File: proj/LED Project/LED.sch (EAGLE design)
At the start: 0 parts

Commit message: Started Schematic
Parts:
- added Q1: (no value), crystal:CRYSTALCTS406
- added R1: 1M, rcl:R-US_R0603
- added U1: ATMEGA328P-AUR, ATMEGA328P-AUR:ATMEGA328P-AUR
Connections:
- new net N$1: Q1.1, R1.2, U1.PB6(PCINT6/XTAL1/TOSC1)
- new net N$2: Q1.2, R1.1, U1.PB7(PCINT7/XTAL2/TOSC2)
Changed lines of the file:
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@@
 <grid distance="0.1" unitdist="inch" unit="inch" style="lines" multiple="1" display="no" altdistance="0.01" altunitdist="inch" altunit="inch"/>
 <layers>
+<layer number="1" name="Top" color="4" fill="1" visible="no" active="no"/>
+<layer number="16" name="Bottom" color="1" fill="1" visible="no" active="no"/>
+<layer number="17" name="Pads" color="2" fill="1" visible="no" active="no"/>
+<layer number="18" name="Vias" color="2" fill="1" visible="no" active="no"/>
+<layer number="19" name="Unrouted" color="6" fill="1" visible="no" active="no"/>
+<layer number="20" name="Dimension" color="15" fill="1" visible="no" active="no"/>
+<layer number="21" name="tPlace" color="7" fill="1" visible="no" active="no"/>
+<layer number="22" name="bPlace" color="7" fill="1" visible="no" active="no"/>
+<layer number="23" name="tOrigins" color="15" fill="1" visible="no" active="no"/>
+<layer number="24" name="bOrigins" color="15" fill="1" visible="no" active="no"/>
+<layer number="25" name="tNames" color="7" fill="1" visible="no" active="no"/>
+<layer number="26" name="bNames" color="7" fill="1" visible="no" active="no"/>
+<layer number="27" name="tValues" color="7" fill="1" visible="no" active="no"/>
+<layer number="28" name="bValues" color="7" fill="1" visible="no" active="no"/>
+<layer number="29" name="tStop" color="7" fill="3" visible="no" active="no"/>
+<layer number="30" name="bStop" color="7" fill="6" visible="no" active="no"/>
+<layer number="31" name="tCream" color="7" fill="4" visible="no" active="no"/>
+<layer number="32" name="bCream" color="7" fill="5" visible="no" active="no"/>
+<layer number="33" name="tFinish" color="6" fill="3" visible="no" active="no"/>
+<layer number="34" name="bFinish" color="6" fill="6" visible="no" active="no"/>
+<layer number="35" name="tGlue" color="7" fill="4" visible="no" active="no"/>
+<layer number="36" name="bGlue" color="7" fill="5" visible="no" active="no"/>
+<layer number="37" name="tTest" color="7" fill="1" visible="no" active="no"/>
+<layer number="38" name="bTest" color="7" fill="1" visible="no" active="no"/>
+<layer number="39" name="tKeepout" color="4" fill="11" visible="no" active="no"/>
+<layer number="40" name="bKeepout" color="1" fill="11" visible="no" active="no"/>
+<layer number="41" name="tRestrict" color="4" fill="10" visible="no" active="no"/>
+<layer number="42" name="bRestrict" color="1" fill="10" visible="no" active="no"/>
+<layer number="43" name="vRestrict" color="2" fill="10" visible="no" active="no"/>
+<layer number="44" name="Drills" color="7" fill="1" visible="no" active="no"/>
+<layer number="45" name="Holes" color="7" fill="1" visible="no" active="no"/>
+<layer number="46" name="Milling" color="3" fill="1" visible="no" active="no"/>
+<layer number="47" name="Measures" color="7" fill="1" visible="no" active="no"/>
+<layer number="48" name="Document" color="7" fill="1" visible="no" active="no"/>
+<layer number="49" name="Reference" color="7" fill="1" visible="no" active="no"/>
+<layer number="51" name="tDocu" color="7" fill="1" visible="no" active="no"/>
+<layer number="52" name="bDocu" color="7" fill="1" visible="no" active="no"/>
 <layer number="88" name="SimResults" color="9" fill="1" visible="yes" active="yes"/>
 <layer number="89" name="SimProbes" color="9" fill="1" visible="yes" active="yes"/>
@@
 </classes>
 <parts>
+<part name="U1" library="ATMEGA328P-AUR" deviceset="ATMEGA328P-AUR" device=""/>
+<part name="R1" library="rcl" library_urn="urn:adsk.eagle:library:334" deviceset="R-US_" device="R0603" package3d_urn="urn:adsk.eagle:package:23555/2" value="1M"/>
+<part name="Q1" library="crystal" library_urn="urn:adsk.eagle:library:204" deviceset="CRYSTAL" device="CTS406" package3d_urn="urn:adsk.eagle:package:12089/1"/>
 </parts>
 <sheets>
@@
 </plain>
 <instances>
+<instance part="U1" gate="G$1" x="73.66" y="40.64"/>
+<instance part="R1" gate="G$1" x="30.48" y="38.1" rot="R90"/>
+<instance part="Q1" gate="G$1" x="20.32" y="38.1" rot="R270"/>
 </instances>
 <busses>
 </busses>
 <nets>
+<net name="N$1" class="0">
+<segment>
+<pinref part="U1" gate="G$1" pin="PB6(PCINT6/XTAL1/TOSC1)"/>
+<wire x1="38.1" y1="40.64" x2="33.02" y2="40.64" width="0.1524" layer="91"/>
+<wire x1="33.02" y1="40.64" x2="33.02" y2="43.18" width="0.1524" layer="91"/>
+<pinref part="R1" gate="G$1" pin="2"/>
+<wire x1="33.02" y1="43.18" x2="30.48" y2="43.18" width="0.1524" layer="91"/>
+<pinref part="Q1" gate="G$1" pin="1"/>
+<wire x1="30.48" y1="43.18" x2="20.32" y2="43.18" width="0.1524" layer="91"/>
+<junction x="30.48" y="43.18"/>
+<wire x1="20.32" y1="40.64" x2="20.32" y2="43.18" width="0.1524" layer="91"/>
+</segment>
+</net>
+<net name="N$2" class="0">
+<segment>
+<pinref part="U1" gate="G$1" pin="PB7(PCINT7/XTAL2/TOSC2)"/>
+<wire x1="38.1" y1="38.1" x2="33.02" y2="38.1" width="0.1524" layer="91"/>
+<wire x1="33.02" y1="38.1" x2="33.02" y2="33.02" width="0.1524" layer="91"/>
+<pinref part="R1" gate="G$1" pin="1"/>
+<wire x1="33.02" y1="33.02" x2="30.48" y2="33.02" width="0.1524" layer="91"/>
+<pinref part="Q1" gate="G$1" pin="2"/>
+<wire x1="20.32" y1="35.56" x2="20.32" y2="33.02" width="0.1524" layer="91"/>
+<wire x1="20.32" y1="33.02" x2="30.48" y2="33.02" width="0.1524" layer="91"/>
+<junction x="30.48" y="33.02"/>
+</segment>
+</net>
 </nets>
 </sheet>
@@
 </schematic>
 </drawing>
+<compatibility>
+<note version="8.2" severity="warning">
+Since Version 8.2, EAGLE supports online libraries. The ids
+of those online libraries will not be understood (or retained)
+with this version.
+</note>
+<note version="8.3" severity="warning">
+Since Version 8.3, EAGLE supports URNs for individual library
+assets (packages, symbols, and devices). The URNs of those assets
+will not be understood (or retained) with this version.
+</note>
+<note version="8.3" severity="warning">
+Since Version 8.3, EAGLE supports the association of 3D packages
+with devices in libraries, schematics, and board files. Those 3D
+packages will not be understood (or retained) with this version.
+</note>
+<note version="8.4" severity="warning">
+Since Version 8.4, EAGLE supports properties for SPICE simulation.
+Probes in schematics and SPICE mapping objects found in parts and library devices
+will not be understood with this version. Update EAGLE to the latest version
+for full support of SPICE simulation.
+</note>
+</compatibility>
 </eagle>

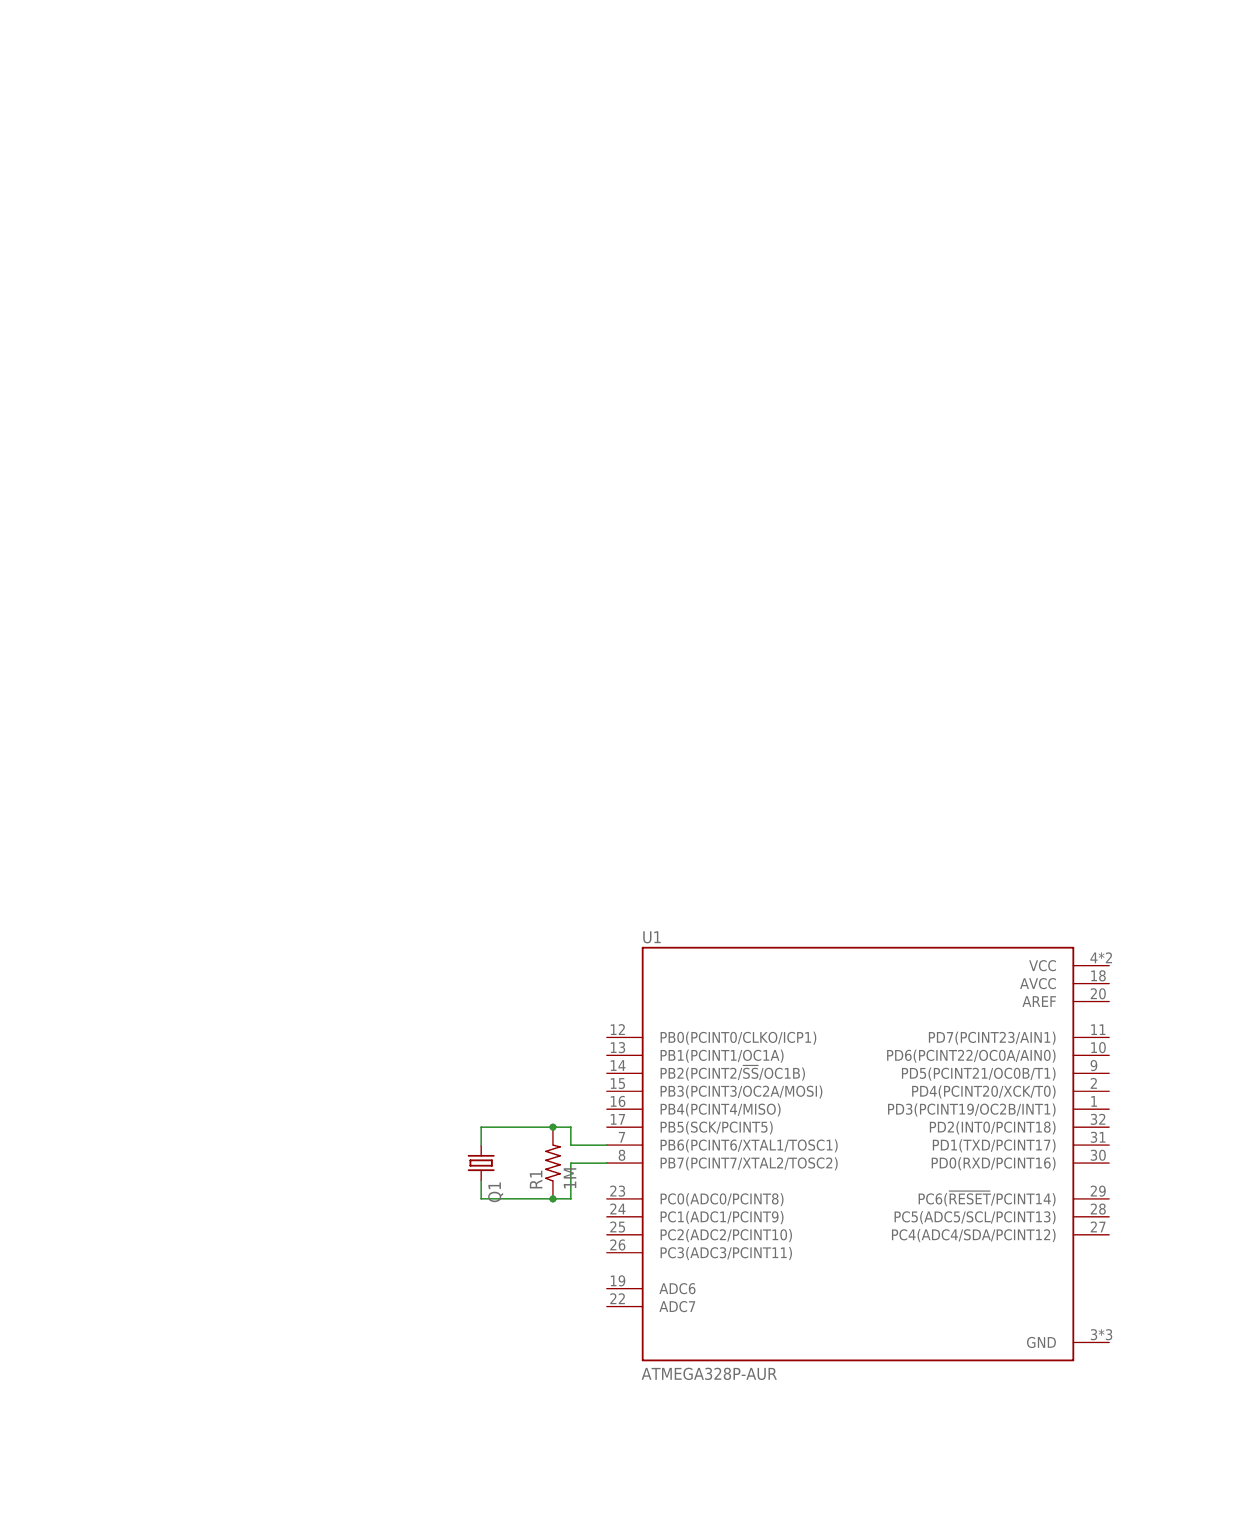
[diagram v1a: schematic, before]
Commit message: Working on the Schematic for a BareBones Arduino
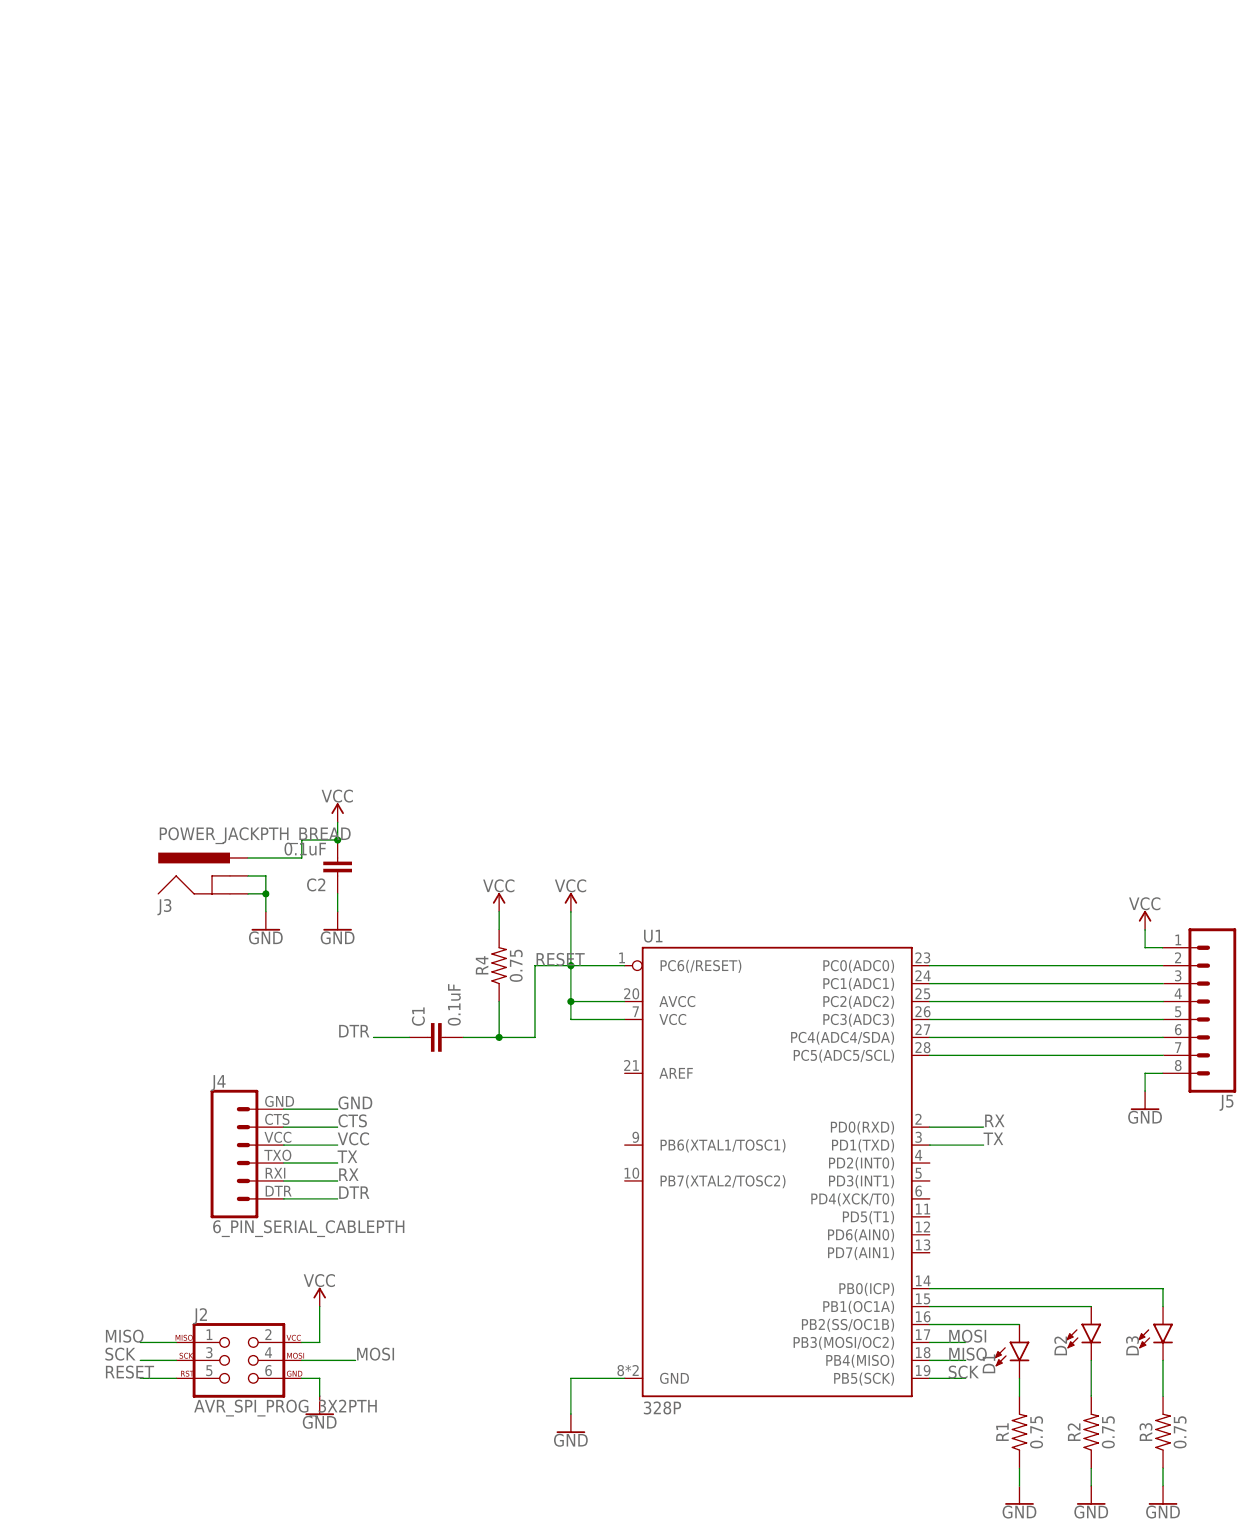
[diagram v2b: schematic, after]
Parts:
- removed Q1: (no value), crystal:CRYSTALCTS406
- added C1, C2: 0.1uF, SparkFun-Capacitors:0.1UF-0402-16V-10%
- added D1, D2, D3: (no value), SparkFun-LED:LED5MM
- added J2: AVR_SPI_PROG_3X2PTH, SparkFun-Connectors:AVR_SPI_PROG_3X2PTH
- added J3: POWER_JACKPTH_BREAD, SparkFun-Connectors:POWER_JACKPTH_BREAD
- added J4: 6_PIN_SERIAL_CABLEPTH, SparkFun-Connectors:6_PIN_SERIAL_CABLEPTH
- added J5: (no value), SparkFun-Connectors:CONN_08"
- added R2, R3, R4: 0.75, SparkFun-Resistors:0.75OHM-0805-1/4W-1%
- R1: value 1M -> 0.75; device rcl:R-US_R0603 -> SparkFun-Resistors:0.75OHM-0805-1/4W-1%
- U1: value ATMEGA328P-AUR -> 328P; device ATMEGA328P-AUR:ATMEGA328P-AUR -> SparkFun-IC-Microcontroller:ATMEGA328P_PDIP
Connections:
- new net CTS: J4.5
- new net DTR: C1.1, J4.1
- new net GND: C2.1, D1.C, D2.C, J2.6, J3.GND, J3.GNDBREAK, J4.6, J5.8, R1.1, R1.2, R2.1, R2.2, R3.1, U1.GND
- new net MISO: J2.1, U1.PB4(MISO)
- new net MOSI: J2.4, U1.PB3(MOSI/OC2)
- new net N$10: D3.A, U1.PB0(ICP)
- new net N$11: D2.A, U1.PB1(OC1A)
- new net N$3: J5.3, U1.PC1(ADC1)
- new net N$4: J5.4, U1.PC2(ADC2)
- new net N$5: J5.5, U1.PC3(ADC3)
- new net N$6: J5.7, U1.PC5(ADC5/SCL)
- new net N$7: J5.6, U1.PC4(ADC4/SDA)
- new net N$8: D1.A, U1.PB2(SS/OC1B)
- new net RESET: C1.2, J2.5, R4.1, U1.AVCC, U1.PC6(/RESET), U1.VCC
- new net RX: J4.2, U1.PD0(RXD)
- new net SCK: J2.3, U1.PB5(SCK)
- new net TX: J4.3, U1.PD1(TXD)
- new net VCC: C2.2, J2.2, J3.PWR, J4.4, J5.1, R4.2
- net N$1: now also J5.2, U1.PC0(ADC0); no longer Q1.1, R1.2, U1.PB6(PCINT6/XTAL1/TOSC1)
- net N$2: now also D3.C, R3.2; no longer Q1.2, R1.1, U1.PB7(PCINT7/XTAL2/TOSC2)
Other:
- moved on the sheet: R1

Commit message: Wired Board
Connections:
- new net N$12: D2.C, R2.2
- new net N$9: D1.C, R1.2
- net GND: no longer D1.C, D2.C, R1.2, R2.2
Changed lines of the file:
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@@
 </segment>
 <segment>
-<pinref part="R1" gate="G$1" pin="2"/>
-<pinref part="R2" gate="G$1" pin="1"/>
-<pinref part="D1" gate="G$1" pin="C"/>
-<wire x1="96.52" y1="7.62" x2="96.52" y2="5.08" width="0.1524" layer="91"/>
-<pinref part="GND1" gate="1" pin="GND"/>
-<wire x1="106.68" y1="-7.62" x2="106.68" y2="-5.08" width="0.1524" layer="91"/>
-</segment>
-<segment>
-<pinref part="R2" gate="G$1" pin="2"/>
 <pinref part="R3" gate="G$1" pin="1"/>
 <pinref part="GND2" gate="1" pin="GND"/>
 <wire x1="116.84" y1="-7.62" x2="116.84" y2="-5.08" width="0.1524" layer="91"/>
-<pinref part="D2" gate="G$1" pin="C"/>
-<wire x1="106.68" y1="10.16" x2="106.68" y2="5.08" width="0.1524" layer="91"/>
 </segment>
 <segment>
@@
 <pinref part="GND6" gate="1" pin="GND"/>
 <wire x1="33.02" y1="7.62" x2="33.02" y2="2.54" width="0.1524" layer="91"/>
+</segment>
+<segment>
+<pinref part="R2" gate="G$1" pin="1"/>
+<pinref part="GND1" gate="1" pin="GND"/>
+<wire x1="106.68" y1="-5.08" x2="106.68" y2="-7.62" width="0.1524" layer="91"/>
 </segment>
 </net>
@@
 </segment>
 </net>
+<net name="N$9" class="0">
+<segment>
+<pinref part="R1" gate="G$1" pin="2"/>
+<pinref part="D1" gate="G$1" pin="C"/>
+<wire x1="96.52" y1="7.62" x2="96.52" y2="5.08" width="0.1524" layer="91"/>
+</segment>
+</net>
+<net name="N$12" class="0">
+<segment>
+<pinref part="D2" gate="G$1" pin="C"/>
+<pinref part="R2" gate="G$1" pin="2"/>
+<wire x1="106.68" y1="10.16" x2="106.68" y2="5.08" width="0.1524" layer="91"/>
+</segment>
+</net>
